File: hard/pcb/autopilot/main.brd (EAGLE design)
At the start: 100 x 65 mm, 195 parts, among them IC1 24AA32ASN, IC2 INA194, IC3 LP2950Z, Q1 IRLML5203, Q2 IRLML5103, T3 BC848, U1 ITG-3200, U2 TMP75DGK, U3 MAG3110, U4 MMA8451Q, U44 BMP085, U5 MAX1236EUA+, X1 USB-SMD-NS

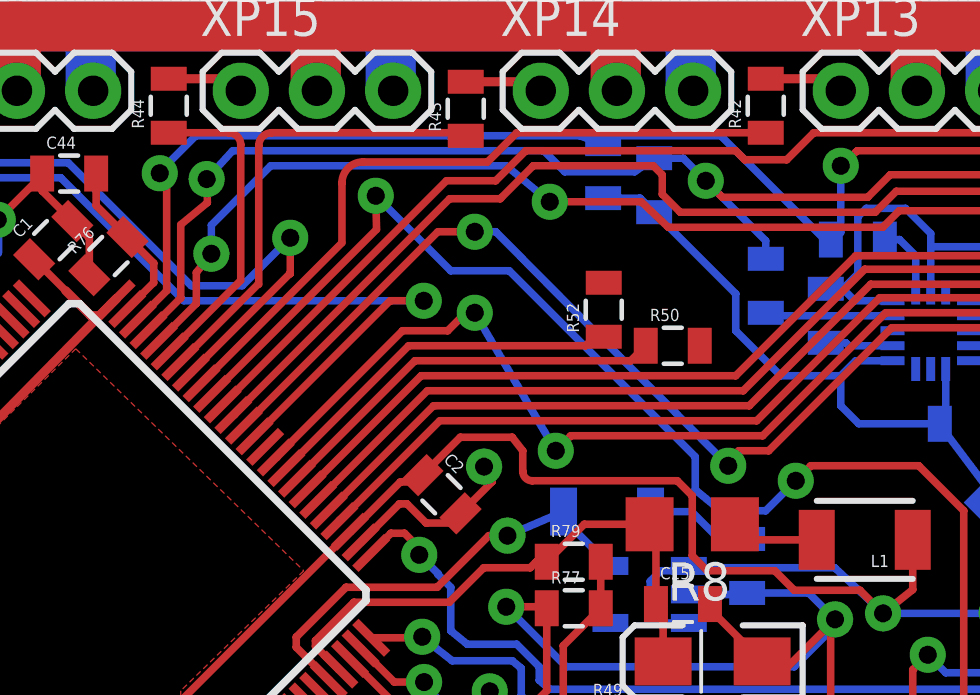
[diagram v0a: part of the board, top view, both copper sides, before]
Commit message: tachometer connected to timer input
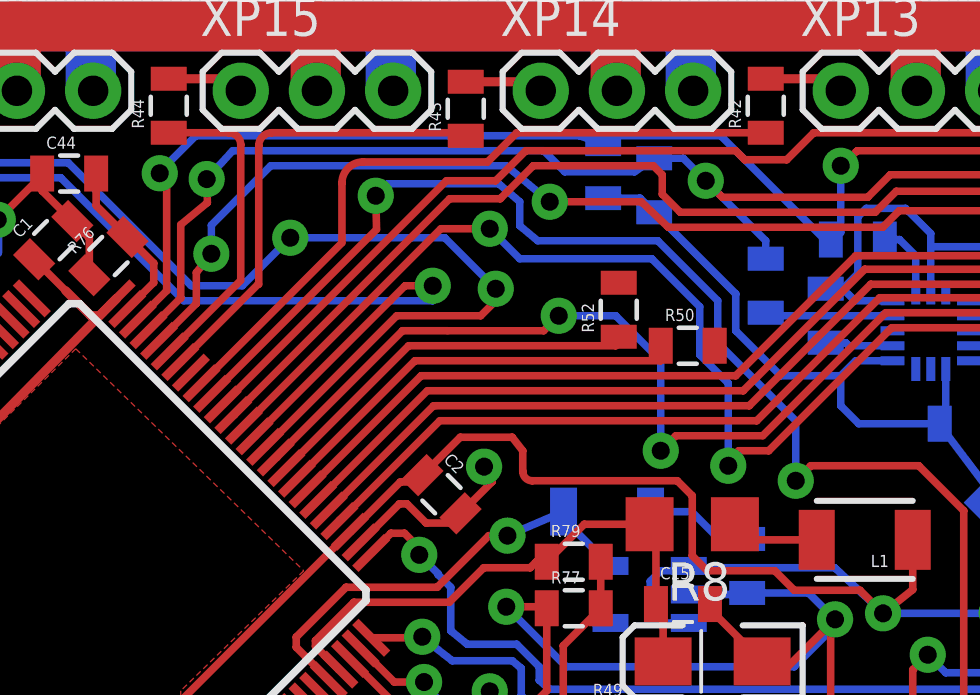
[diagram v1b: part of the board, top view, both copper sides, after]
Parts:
- moved R50 0.50 mm to (70.9, 53.5)
- moved R52 0.50 mm to (68.6, 54.7)
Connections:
- net TACHOMETER: now also DD2.36; no longer DD2.43
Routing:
- net TACHOMETER: track 94.1 -> 105.8 mm, vias 4 -> 5
- net MAG_INT: track 73.7 -> 76.3 mm
- net BOOT_1: track 107.1 -> 108.4 mm
- net ITG-3200_INT: track 51.9 -> 53.2 mm
- net RECEIVER_PPM: track 50.4 -> 51.4 mm
- net N$45: track 12.4 -> 13.3 mm
- net N$49: track 13.5 -> 14.3 mm
